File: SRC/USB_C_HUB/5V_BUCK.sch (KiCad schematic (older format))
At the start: 11 parts

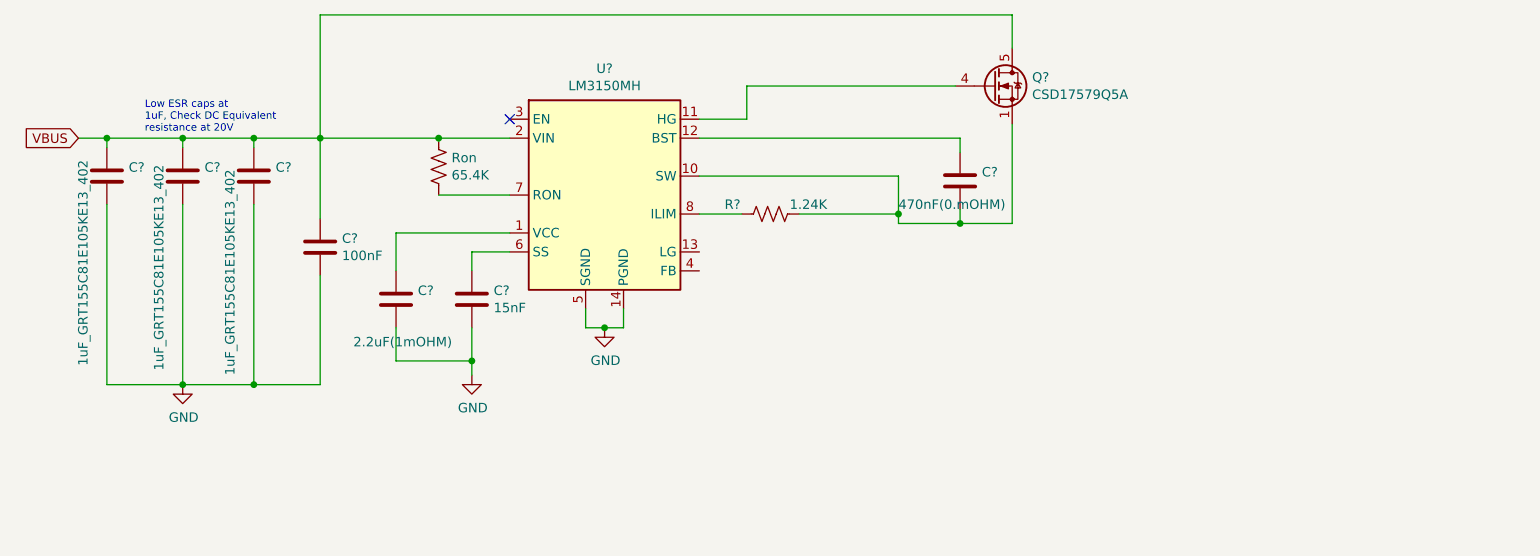
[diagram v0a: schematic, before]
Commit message: With ST_PD controller, Buck $ Boost regulators
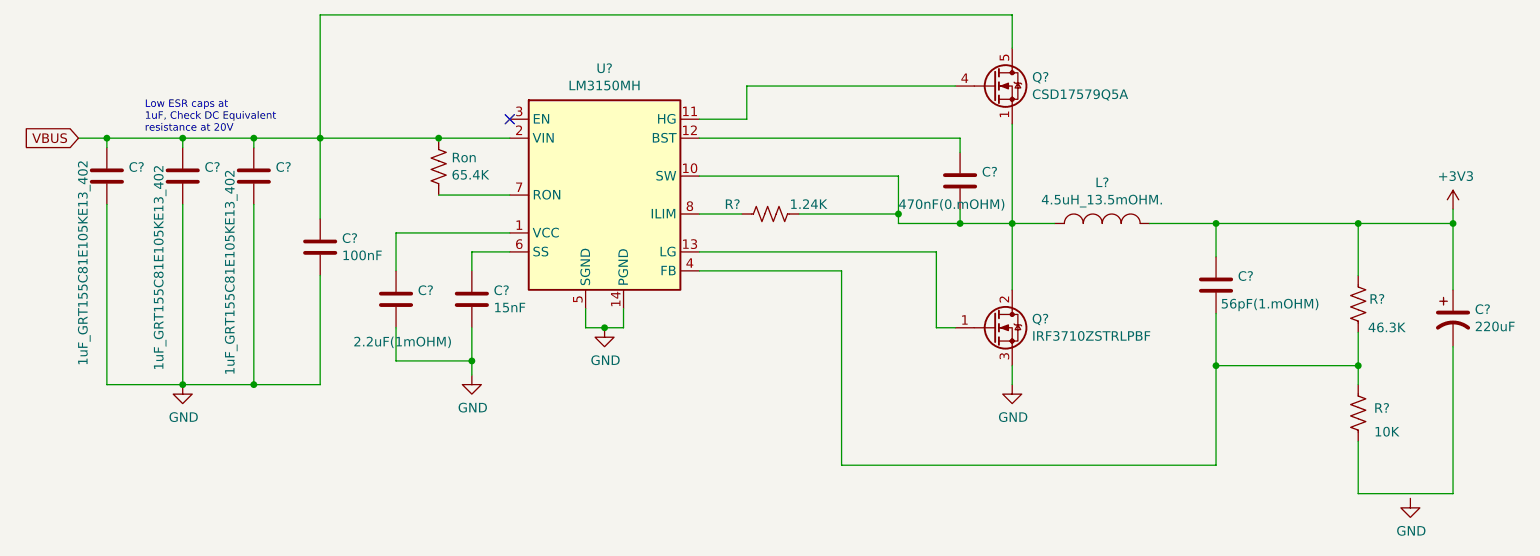
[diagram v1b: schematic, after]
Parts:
- added C?: 56pF(1.mOHM), symbol Device:C
- added C?: 220uF, symbol Device:CP1
- added L?: 4.5uH_13.5mOHM., symbol OLIMEX_RCL:INDUCTOR_SMALL
- added Q?: IRF3710ZSTRLPBF, Package_TO_SOT_THT:TO-220-3_Vertical, symbol Transistor_FET:IRF3205
- added R?: 46.3K, symbol Device:R_US
- added R?: 10K, symbol Device:R_US
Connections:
- net GND: now also Q?.3 (S)
- net at C?.2, Q?.1 (S), Q?.2 (S)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: now also L?.1, Q?.2 (D)
- net at U?.13 (LG): now also Q?.1 (G)
- net at U?.4 (FB): now also C?.2, R?.1, R?.2
- new net: C?.2, R?.1
- new net +3V3: C?.1, C?.1, L?.2, R?.2
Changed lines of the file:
@@
 	4700 2850 4700 2750
 Connection ~ 4600 2850
+$Comp
+L Transistor_FET:IRF3205 Q?
+U 1 1 61F7E29D
+P 6650 2850
+F 0 "Q?" H 6854 2896 50  0000 L CNN
+F 1 "IRF3710ZSTRLPBF" H 6854 2805 50  0000 L CNN
+F 2 "Package_TO_SOT_THT:TO-220-3_Vertical" H 6900 2775 50  0001 L CIN
+F 3 "http://www.irf.com/product-info/datasheets/data/irf3205.pdf" H 6650 2850 50  0001 L CNN
+	1    6650 2850
+	1    0    0    -1
+$EndComp
+Wire Wire Line
+	5100 2450 6350 2450
+Wire Wire Line
+	6350 2450 6350 2850
+Wire Wire Line
+	6350 2850 6450 2850
+$Comp
+L OLIMEX_RCL:INDUCTOR_SMALL L?
+U 1 1 61F81398
+P 7225 2300
+F 0 "L?" H 7225 2515 50  0000 C CNN
+F 1 "4.5uH_13.5mOHM." H 7225 2424 50  0000 C CNN
+F 2 "" H 7225 2300 60  0000 C CNN
+F 3 "" H 7225 2300 60  0000 C CNN
+	1    7225 2300
+	1    0    0    -1
+$EndComp
+Wire Wire Line
+	6750 2300 6750 2650
+Connection ~ 6750 2300
+Wire Wire Line
+	6975 2300 6750 2300
+$Comp
+L Device:C C?
+U 1 1 61F860EE
+P 7825 2625
+F 0 "C?" H 7940 2671 50  0000 L CNN
+F 1 "56pF(1.mOHM)" H 7850 2525 50  0000 L CNN
+F 2 "" H 7863 2475 50  0001 C CNN
+F 3 "~" H 7825 2625 50  0001 C CNN
+F 4 "C1005C0G1H560J050BA" H 7825 2625 50  0001 C CNN "Mfr No."
+	1    7825 2625
+	1    0    0    -1
+$EndComp
+Wire Wire Line
+	7475 2300 7825 2300
+Wire Wire Line
+	7825 2300 7825 2475
+$Comp
+L OLIMEX_Power:GND #PWR?
+U 1 1 61F8B931
+P 6750 3150
+F 0 "#PWR?" H 6750 2900 50  0001 C CNN
+F 1 "GND" H 6755 2977 50  0000 C CNN
+F 2 "" H 6750 3150 60  0000 C CNN
+F 3 "" H 6750 3150 60  0000 C CNN
+	1    6750 3150
+	1    0    0    -1
+$EndComp
+Wire Wire Line
+	6750 3150 6750 3050
+$Comp
+L Device:R_US R?
+U 1 1 61F8DE0C
+P 8575 2725
+F 0 "R?" H 8475 2700 50  0000 C CNN
+F 1 "46.3K" H 8425 2850 50  0000 C CNN
+F 2 "" V 8615 2715 50  0001 C CNN
+F 3 "~" H 8575 2725 50  0001 C CNN
+	1    8575 2725
+	-1   0    0    1
+$EndComp
+Wire Wire Line
+	8575 2575 8575 2300
+Wire Wire Line
+	8575 2300 7825 2300
+Connection ~ 7825 2300
+$Comp
+L Device:R_US R?
+U 1 1 61F90FEA
+P 8575 3300
+F 0 "R?" H 8450 3275 50  0000 C CNN
+F 1 "10K" H 8425 3400 50  0000 C CNN
+F 2 "" V 8615 3290 50  0001 C CNN
+F 3 "~" H 8575 3300 50  0001 C CNN
+	1    8575 3300
+	-1   0    0    1
+$EndComp
+Wire Wire Line
+	8575 3450 8575 3725
+Wire Wire Line
+	7825 3050 8575 3050
+Wire Wire Line
+	7825 2775 7825 3050
+Wire Wire Line
+	8575 2875 8575 3050
+Connection ~ 8575 3050
+Wire Wire Line
+	8575 3050 8575 3150
+$Comp
+L Device:CP1 C?
+U 1 1 61F96026
+P 9075 2800
+F 0 "C?" H 9190 2846 50  0000 L CNN
+F 1 "220uF" H 9190 2755 50  0000 L CNN
+F 2 "" H 9075 2800 50  0001 C CNN
+F 3 "~" H 9075 2800 50  0001 C CNN
+	1    9075 2800
+	1    0    0    -1
+$EndComp
+Wire Wire Line
+	9075 2650 9075 2300
+Wire Wire Line
+	9075 2300 8575 2300
+Connection ~ 8575 2300
+Wire Wire Line
+	9075 2950 9075 3725
+Wire Wire Line
+	8575 3725 9075 3725
+$Comp
+L OLIMEX_Power:GND #PWR?
+U 1 1 61F9A0A2
+P 8850 3750
+F 0 "#PWR?" H 8850 3500 50  0001 C CNN
+F 1 "GND" H 8855 3577 50  0000 C CNN
+F 2 "" H 8850 3750 60  0000 C CNN
+F 3 "" H 8850 3750 60  0000 C CNN
+	1    8850 3750
+	1    0    0    -1
+$EndComp
+Wire Wire Line
+	7825 3050 7825 3575
+Wire Wire Line
+	7825 3575 5850 3575
+Wire Wire Line
+	5850 3575 5850 2550
+Wire Wire Line
+	5850 2550 5100 2550
+Connection ~ 7825 3050
+$Comp
+L power:+3V3 #PWR?
+U 1 1 61F9D8B8
+P 9075 2225
+F 0 "#PWR?" H 9075 2075 50  0001 C CNN
+F 1 "+3V3" H 9090 2398 50  0000 C CNN
+F 2 "" H 9075 2225 50  0001 C CNN
+F 3 "" H 9075 2225 50  0001 C CNN
+	1    9075 2225
+	1    0    0    -1
+$EndComp
+Wire Wire Line
+	9075 2225 9075 2300
+Connection ~ 9075 2300
 $EndSCHEMATC
